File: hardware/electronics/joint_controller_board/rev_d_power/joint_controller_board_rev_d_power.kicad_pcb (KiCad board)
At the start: 2 copper layers, 40 x 60 mm, 41 parts, among them J1 J_IFACE, J2 J_PWR_IN_RAW, J4 J_PWR_OUT_SW, Q1 BSC016N06NS, Q2 BSC016N06NS, U1 TPS2492PW, U2 LMR36520ADDA, U3 TLV75533PDBV

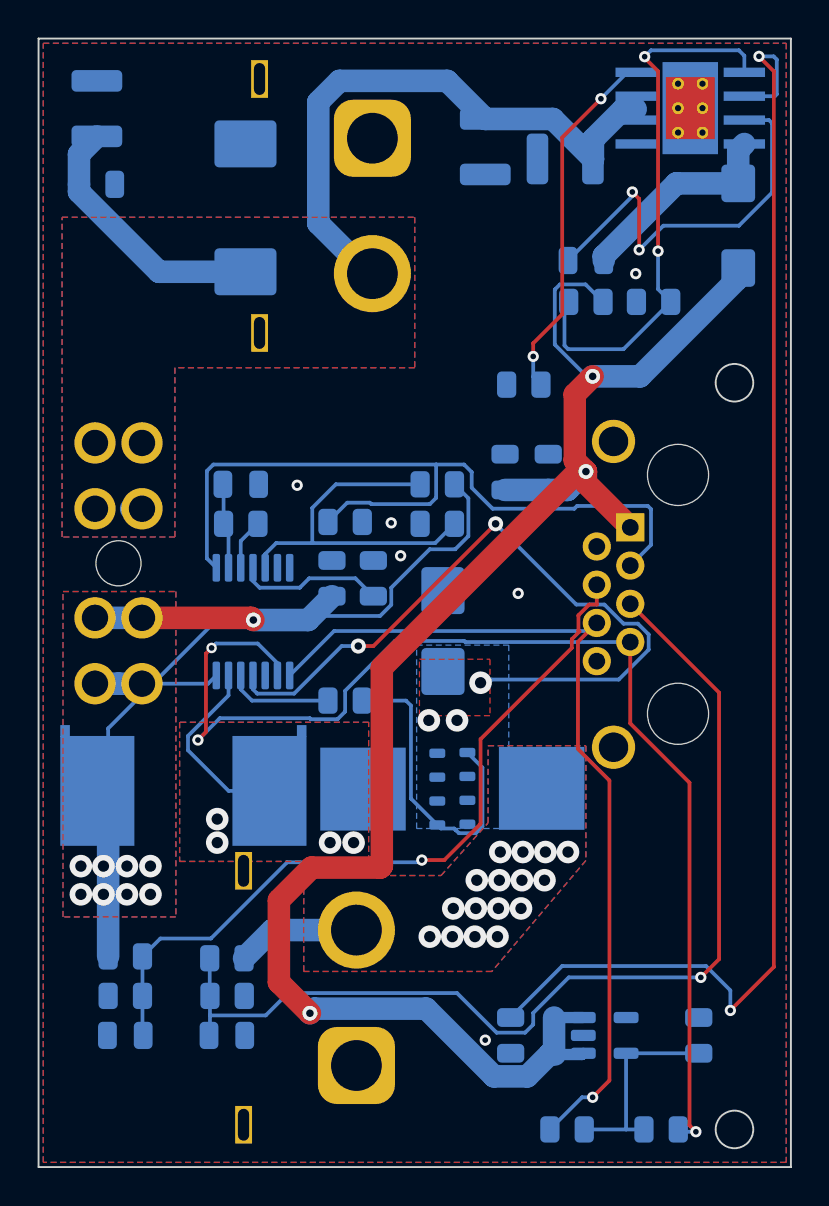
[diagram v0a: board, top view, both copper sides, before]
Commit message: feat(rev_d_power): move branch fuse off-board to upstream PDU (Option C1)
Remove on-board F1 fuse + holder from schematic and layout. Per-joint 30A ATO
slow-blow now lives on the upstream PDU / battery distribution board. Saves
~24mm vertical clearance inside joint enclosure (resolved mechanical fit-check
blocker) and protects the full cable run rather than only the PCB. On-board
fast protection preserved via TPS2492 current-limit (~40A latch-off).

Net renames: 24V_POST_F1 -> 24V_RAW (unified), VIN_POST_F1_MON -> VIN_RAW_MON.
RJ45 pin 4 signal name and related schematic descriptions updated accordingly
in ARCHITECTURE.md and COMPONENT_SELECTION.md.

ERC 0/0, DRC 0 violations (2 preexisting XT60 J2/J4 gender-swap warnings
unchanged).

Signed-off-by: graceful-kinematics <info@aliahumanoid.com>
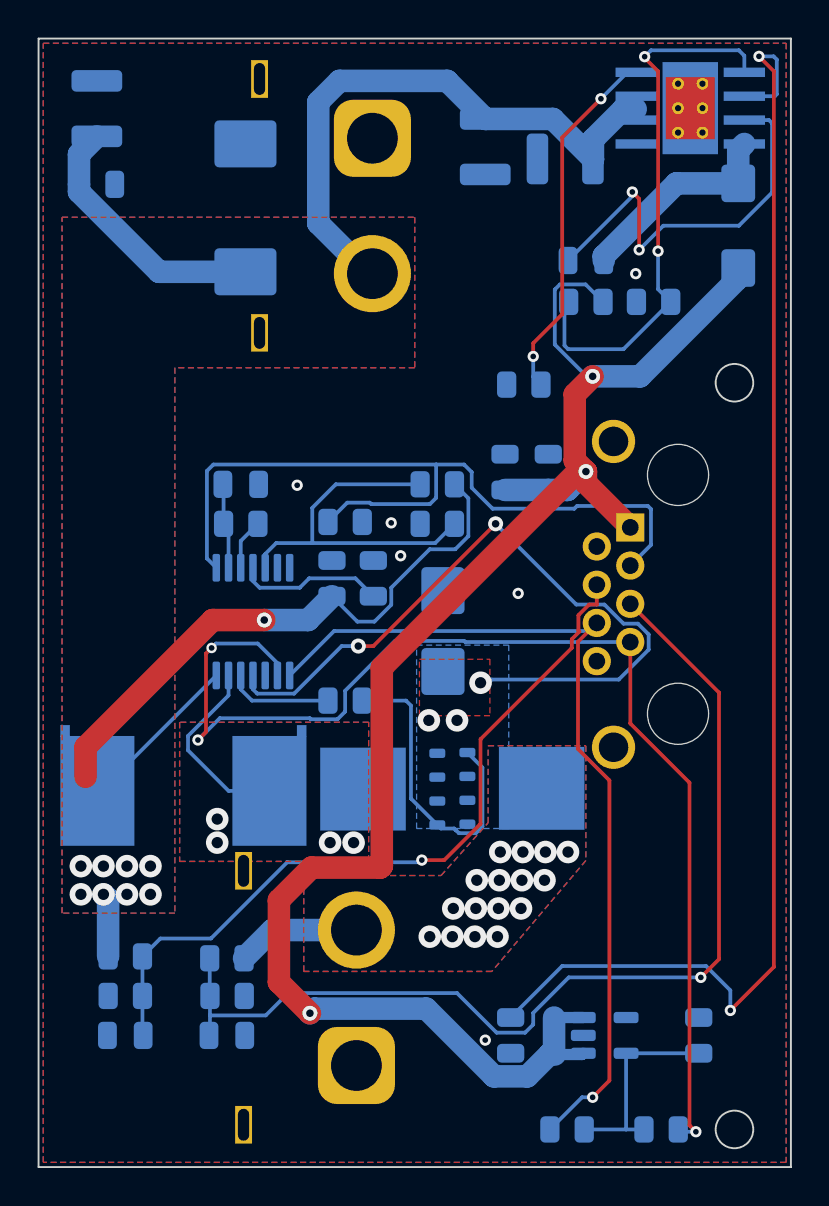
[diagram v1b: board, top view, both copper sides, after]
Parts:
- removed F1: 30A, rev_d_power_footprints:FuseHolder_Blade_ATO_Littelfuse_FLR_178.6165
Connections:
- net VIN_POST_F1_MON renamed VIN_RAW_MON
- C24 pad 2: 24V_POST_F1 -> 24V_RAW
- R11 pad 1: 24V_POST_F1 -> 24V_RAW
- R31 pad 1: 24V_POST_F1 -> 24V_RAW
- R4 pad 1: 24V_POST_F1 -> 24V_RAW
- U1 pad 14: 24V_POST_F1 -> 24V_RAW
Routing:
- net 24V_POST_F1: track 70.3 -> 0.00 mm, vias 9 -> 0
- net 24V_RAW: track 46.8 -> 91.3 mm, vias 0 -> 9
- removed copper zone on B.Cu, net 24V_POST_F1
- removed copper zone on F.Cu, net 24V_POST_F1

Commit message: feat(rev_d_power): remove raw daisy-chain J3, align XT60 library prefix
Drop the J3 XT60PW-F raw-pass-through connector and its dedicated copper.
The board now has a single raw-input (J2 XT60PW-F) and a single switched
motor output (J4 XT60PW-M). Branch fan-out is handled by the upstream PDU,
consistent with Option C1 external fusing landed in the previous commit.

Also align the J2/J4 footprint library references with the matching
schematic symbols by adding the explicit Connector_AMASS: prefix. Clears
the last two footprint_symbol_mismatch DRC schematic-parity warnings.

Docs updated:
- ARCHITECTURE.md: External Interfaces lists only J_PWR_IN_RAW and
  J_PWR_OUT_SW; Architecture Decision 1 rewritten as "No on-board raw
  daisy-chain output"; power diagram, 6 "Raw daisy-chain sizing" section,
  and test-point list trimmed accordingly; IMON note: pin budget full, not
  routed to RJ45 in this revision.
- COMPONENT_SELECTION.md: topology reflects no raw daisy-chain.
- README.md: board size corrected to 40x60 mm; J2/J4 gender listed; ERC 0/0
  and DRC 0 documented.

ERC 0/0. DRC: 0 violations, 0 unconnected pads, 0 footprint errors.
Board size 40 x 60 mm. BOM 27 rows (was 28 with J3).

Signed-off-by: graceful-kinematics <info@aliahumanoid.com>
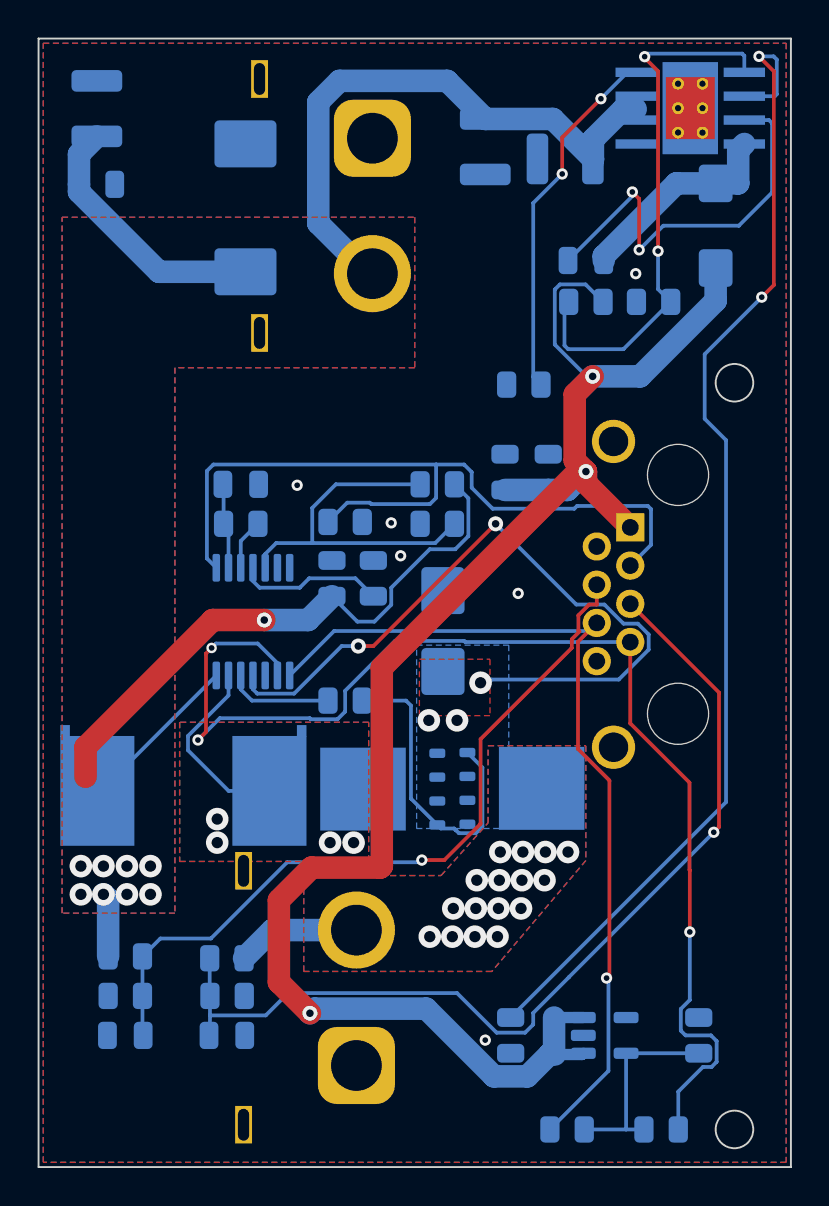
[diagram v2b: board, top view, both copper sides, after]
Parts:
- J2: footprint AMASS_XT60PW-F_1x02_P7.20mm_Horizontal -> Connector_AMASS:AMASS_XT60PW-F_1x02_P7.20mm_Horizontal
- J4: footprint AMASS_XT60PW-M_1x02_P7.20mm_Horizontal -> Connector_AMASS:AMASS_XT60PW-M_1x02_P7.20mm_Horizontal
- moved L1 1.20 mm to (156.0, 70.0)
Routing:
- net /U2_VCC: track 71.1 -> 62.8 mm
- net VOUT_POST_FET_MON: track 55.4 -> 51.3 mm
- net FAULT_N: track 64.2 -> 65.9 mm
